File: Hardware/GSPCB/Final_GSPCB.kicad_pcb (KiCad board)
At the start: 2 copper layers, 80 x 69.8 mm, 84 parts, among them J2 Conn_01x02_Socket, U14 TXB0106RGYR, U4 LD39200PU33R, U7 TPS51386RJNR

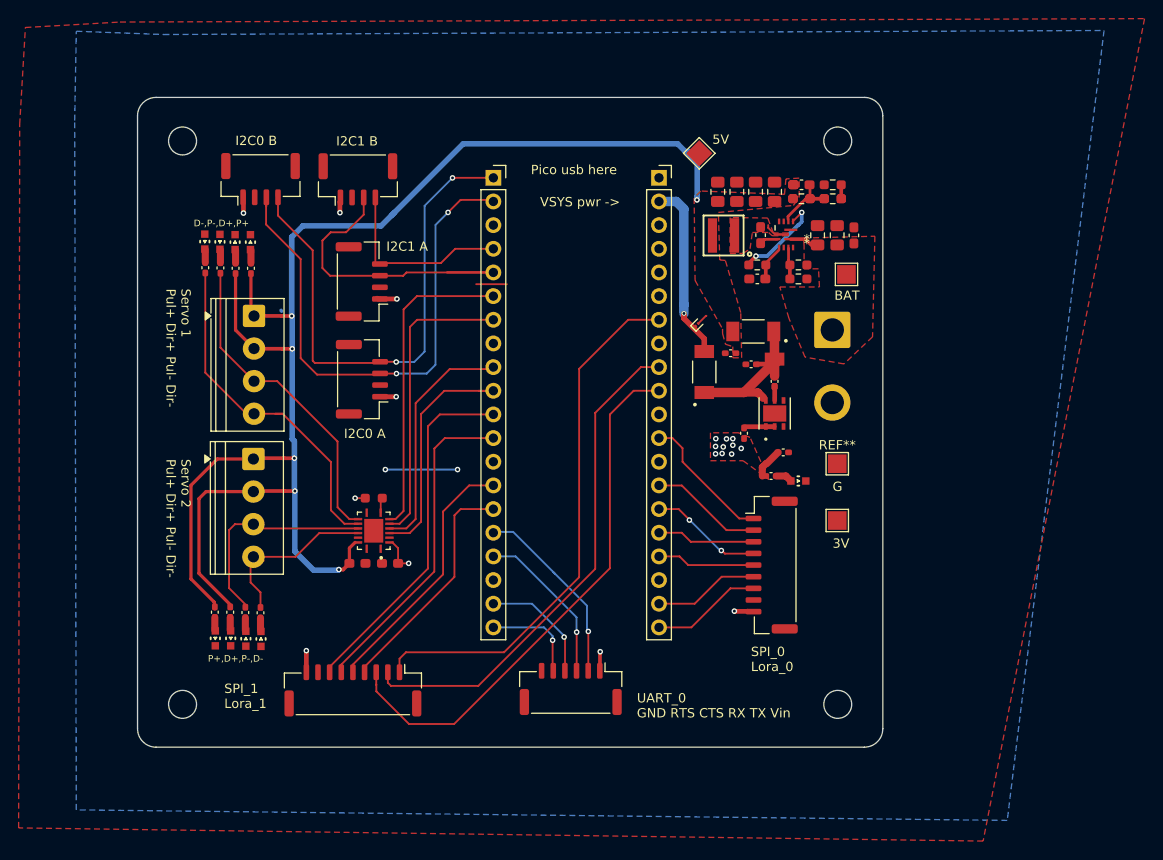
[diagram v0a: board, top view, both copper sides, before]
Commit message: Quick touchups and final review for ordering, needs BoM confirmation
- Rerouted a couple signal lines on bottom layer for spacing and groundplane placement
- Touched up a few copper pour boundaries for simplified component placement
- Added more silkscreen labels and aligned with components, including I2C port pinout
- Standardized (larger) vias for JLCPCB ordering
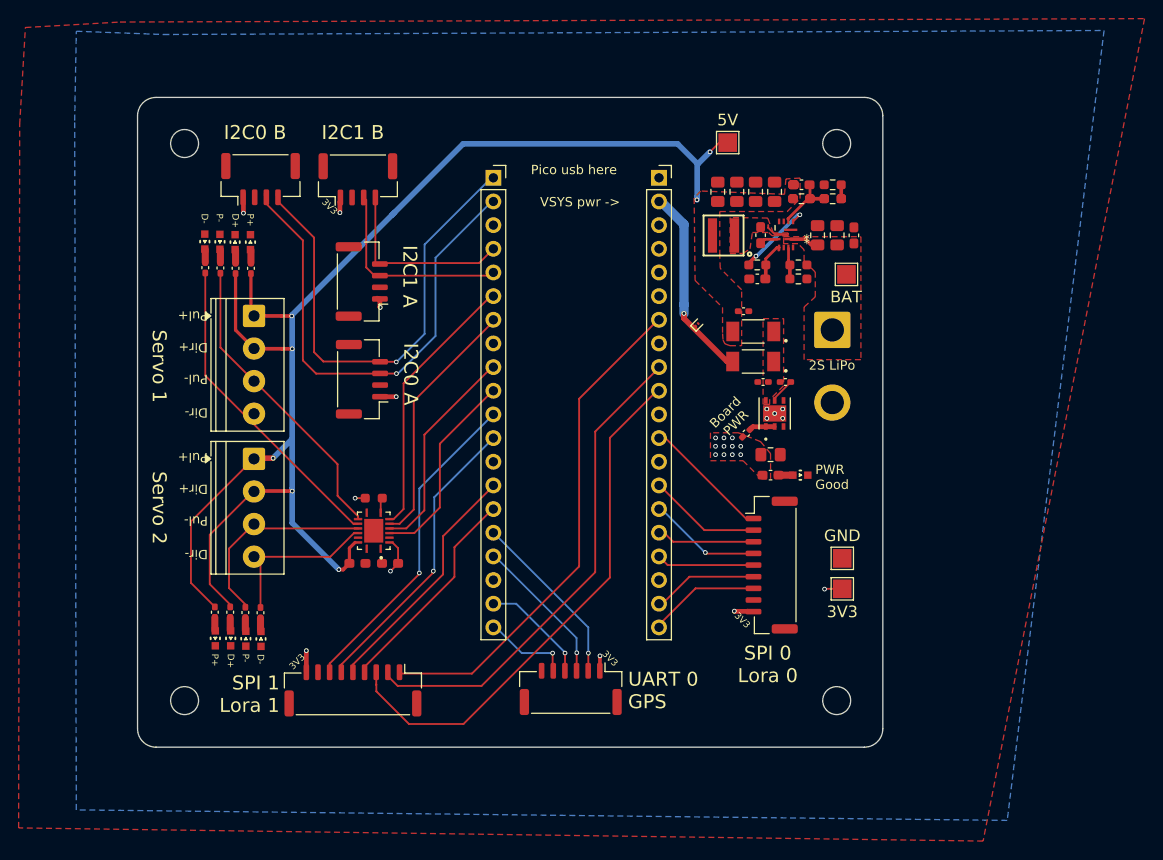
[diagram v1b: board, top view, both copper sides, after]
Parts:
- removed the ? at (113.4, 87.2)
- removed the ? at (113.4, 84.2)
- removed the ? at (113.4, 86.1)
- C16: footprint Capacitor_SMD:C_0402_1005Metric_Pad0.74x0.62mm_HandSolder -> Capacitor_SMD:C_0805_2012Metric_Pad1.18x1.45mm_HandSolder
- R15: footprint Capacitor_SMD:C_0402_1005Metric_Pad0.74x0.62mm_HandSolder -> Capacitor_SMD:C_0603_1608Metric_Pad1.08x0.95mm_HandSolder
- moved REF** 10.2 mm to (120.7, 105.6)
- moved REF** 7.35 mm to (120.7, 108.9)
- moved D4 5.37 mm to (111.1, 84.5), turned to 180 degrees
- moved C21 4.72 mm to (110.0, 79.1), turned to 0 degrees
- moved REF** 3.26 mm to (108.3, 61.0), turned to -90 degrees
- moved C15 2.29 mm to (112.2, 86.7)
- moved C16 1.39 mm to (113.0, 94.5)
- moved R4 1.17 mm to (114.5, 86.7), turned to 0 degrees
- moved D11 0.66 mm to (116.2, 96.7)
- moved H2 0.46 mm to (50.0, 120.9)
- moved H2 0.42 mm to (120.0, 120.9)
- moved H2 0.35 mm to (50.0, 61.1)
- moved H2 0.30 mm to (120.0, 61.1)
- moved R21 0.24 mm to (110.3, 92.2), turned to -135 degrees
- moved R15 0.11 mm to (113.0, 96.7)
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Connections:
- REF** pad 8: (no net) -> GND
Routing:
- net (no net): track 663.4 -> 619.8 mm, vias 10 -> 9
- net /VREG_3V3: track 139.2 -> 119.4 mm, vias 19 -> 21
- net Net-(U4-IN): track 18.6 -> 0.12 mm
- net GND: track 12.2 -> 0.00 mm, vias 2 -> 5
- net /VREG_5V: track 170.5 -> 159.7 mm, vias 6 -> 7
- net Net-(D11-Pad2): track 73.4 -> 68.7 mm
- net /Power Management/VBUS: track 19.3 -> 21.0 mm
- net Net-(U7-PG): track 9.89 -> 8.68 mm
- net Net-(U4-EN): track 1.78 -> 2.70 mm
- net Net-(U7-VCC): track 3.42 -> 4.14 mm
- added copper zone on F.Cu, net Net-(U4-IN)
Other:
- board text added: "2S LiPo"
- board text added: "3V3"
- board text added: "Board PWR"
- board text added: "D+"
- board text added: "D-"
- board text added: "Dir+"
- board text added: "Dir-"
- board text added: "GND"
- board text added: "I2C0/1 - Pin Order 3V3 GND SCL SDA"
- board text added: "LORA 0 - Pin Order Reset CSn TX RX SCK G0 EN GND Vin"
- board text added: "LORA 1 - Pin Order En G0 Reset TX SCK CSn RX GND 3V3"
- board text added: "P+"
- board text added: "P-"
- board text added: "PWR Good"
- board text added: "Pul+"
- board text added: "Pul-"
- board text added: "SPI 0 Lora 0"
- board text added: "SPI 1 Lora 1"
- board text added: "Servo 1"
- board text added: "Servo 2"
- board text added: "UART 0 - Pin Order GND RTS CTS RX TX 3V3"
- board text added: "UART 0 GPS"
- board text removed: "3V"
- board text removed: "D-,P-,D+,P+"
- board text removed: "G"
- board text removed: "LORA_1 Pin use in order En, G0, Reset, TX, SCK, CSn, RX, GND, Vin"
- board text removed: "Lora_0 Pin use in order Reset CSn TX RX SCK G0 EN GND Vin"
- board text removed: "P+,D+,P-,D-"
- board text removed: "SPI_0 Lora_0"
- board text removed: "SPI_1 Lora_1"
- board text removed: "Servo 1 Pul+ Dir+ Pul- Dir-"
- board text removed: "Servo 2 Pul+ Dir+ Pul- Dir-"
- board text removed: "UART_0 GND RTS CTS RX TX Vin"

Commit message: Final Rev1 ordered 4/27/26
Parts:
- added D3: PMEG3050EP_115, footprints_logger:DIO_PMEG3050EP_115, F.Cu at (101.0, 61.1)
- moved REF** 0.06 mm to (105.1, 80.5)
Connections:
- D11 pad 2: GND -> /VREG_5V (x4)
- REF** pad 1: (no net) -> /Power Management/VBUS
- REF** pad 2: /Power Management/VBUS -> VSYS
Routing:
- net /VREG_5V: track 159.7 -> 205.1 mm, vias 7 -> 10
- net VSYS: track 0.00 -> 7.50 mm
- net /Power Management/VBUS: track 21.0 -> 23.4 mm
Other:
- board text added: "(-) signals active LOW"
- board text added: "LORA 0 - Pin Order Reset CSn TX RX SCK G0 EN GND 3V3"
- board text added: "Power Good"
- board text added: "Raspberry Pi Pico"
- board text added: "VSYS pwr -"
- board text removed: "LORA 0 - Pin Order Reset CSn TX RX SCK G0 EN GND Vin"
- board text removed: "PWR Good"
- board text removed: "Pico usb here"
- board text removed: "VSYS pwr ->"
